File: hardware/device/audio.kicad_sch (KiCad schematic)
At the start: 33 parts, among them J4 HP_OUT, J5 AUDIO_EXP, J8 LINE_OUT, J9 LINE_IN, U24 MIC, U28 TS5A23159RSE, U29 NAU88C22YG, U30 TS5A23159RSE

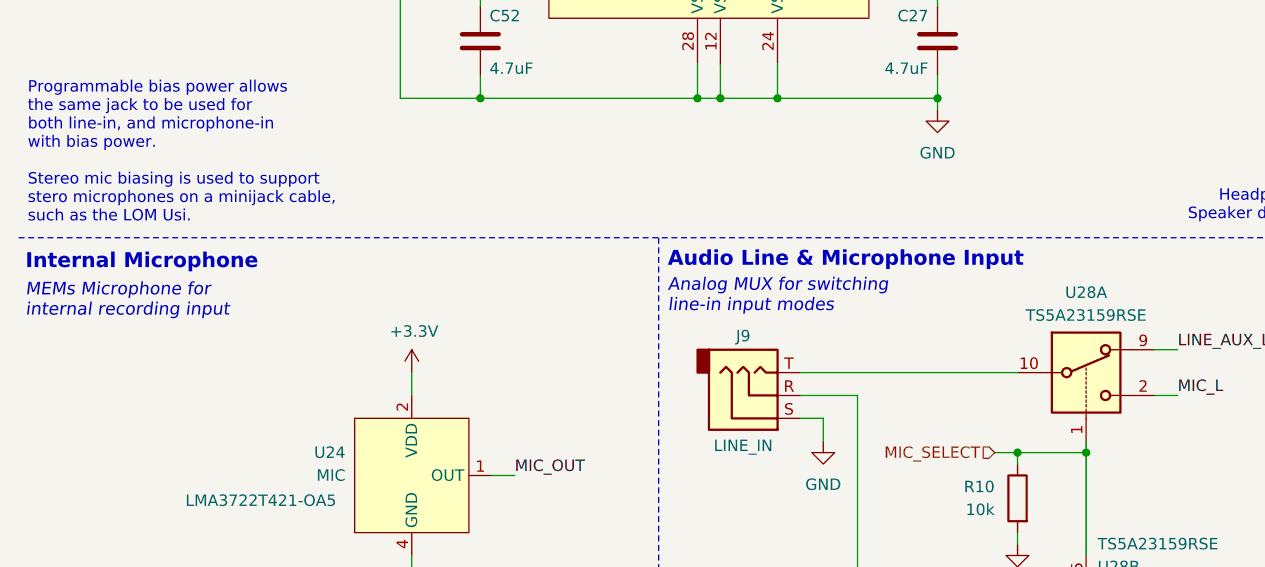
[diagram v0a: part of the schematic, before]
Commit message: feat: start routing keyswitch pads
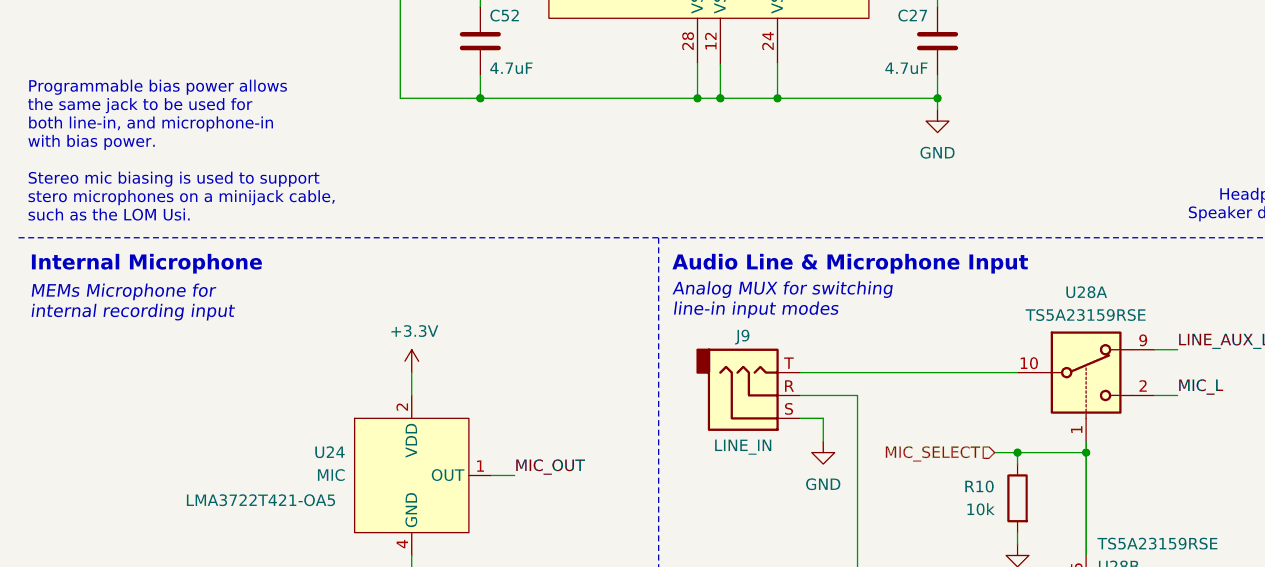
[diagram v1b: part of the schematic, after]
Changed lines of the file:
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@@
 	(text "MEMs Microphone for\ninternal recording input"
 		(exclude_from_sim no)
-		(at 12.954 151.384 0)
+		(at 13.462 151.638 0)
 		(effects
 			(font
@@
 	(text "Analog MUX for switching\nline-in input modes"
 		(exclude_from_sim no)
-		(at 84.328 150.876 0)
+		(at 84.836 151.384 0)
 		(effects
 			(font
@@
 	(text "Audio Line & Microphone Input"
 		(exclude_from_sim no)
-		(at 84.328 147.828 0)
+		(at 84.836 148.336 0)
 		(effects
 			(font
@@
 	(text "Internal Microphone"
 		(exclude_from_sim no)
-		(at 12.954 148.082 0)
-		(effects
-			(font
+		(at 13.462 148.336 0)
+		(effects
+			(font

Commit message: feat: audio system routing
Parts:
- removed C8: 0.1uF, Capacitor_SMD:C_0201_0603Metric, symbol Device:C_Small
- removed R11: 10k, Resistor_SMD:R_0201_0603Metric, symbol Device:R
- removed U30: TS5A23159RSE, Package_DFN_QFN:Texas_R-PUQFN-N10, symbol Analog_Switch:TS5A23159RSE
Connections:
- net LINE_AUX_L is gone; now on net AUX_L: U28.9
- net LINE_AUX_R is gone; now on net AUX_R: U28.7
- net CODEC.ADCDAT: no longer J5.5
- net CODEC.BCLK: no longer J5.9
- net CODEC.DACDAT: no longer J5.3
- net CODEC.LRCLK: no longer J5.7
- net CODEC.MCLK: no longer J5.11
- net EXP_CODEC.ADCDAT: now also J5.5; no longer J5.12
- net EXP_CODEC.BCLK: now also J5.9; no longer J5.16
- net EXP_CODEC.DACDAT: now also J5.3; no longer J5.10
- net EXP_CODEC.LRCLK: now also J5.7; no longer J5.14
- net EXP_CODEC.MCLK: now also J5.11; no longer J5.18
- net CODEC_IRQ: now reaches U29.6 (RLIN/GPIO3)
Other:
- note removed: "Aux-In Selection"

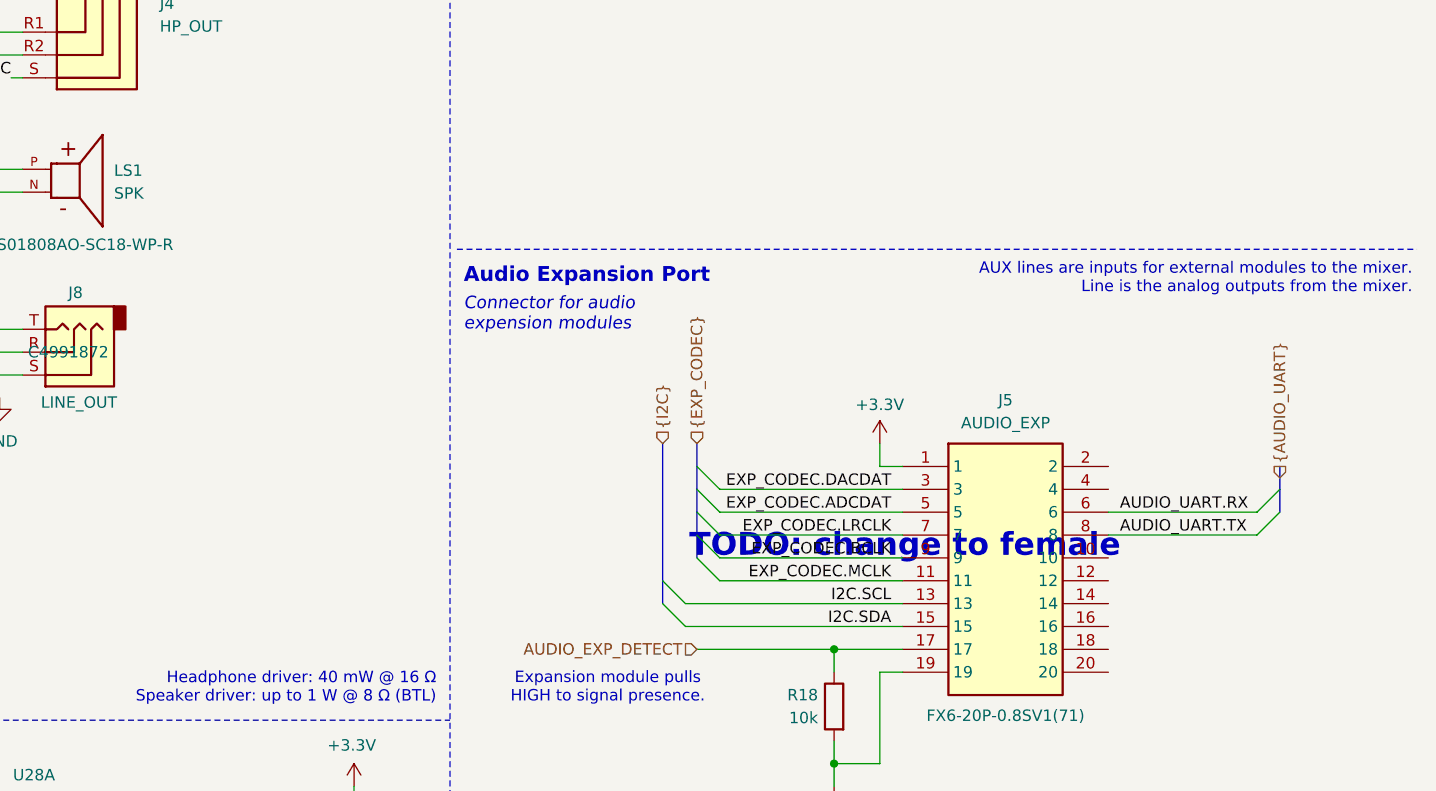
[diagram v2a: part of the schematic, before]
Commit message: feat: various routing, footprint and schematic cleanup
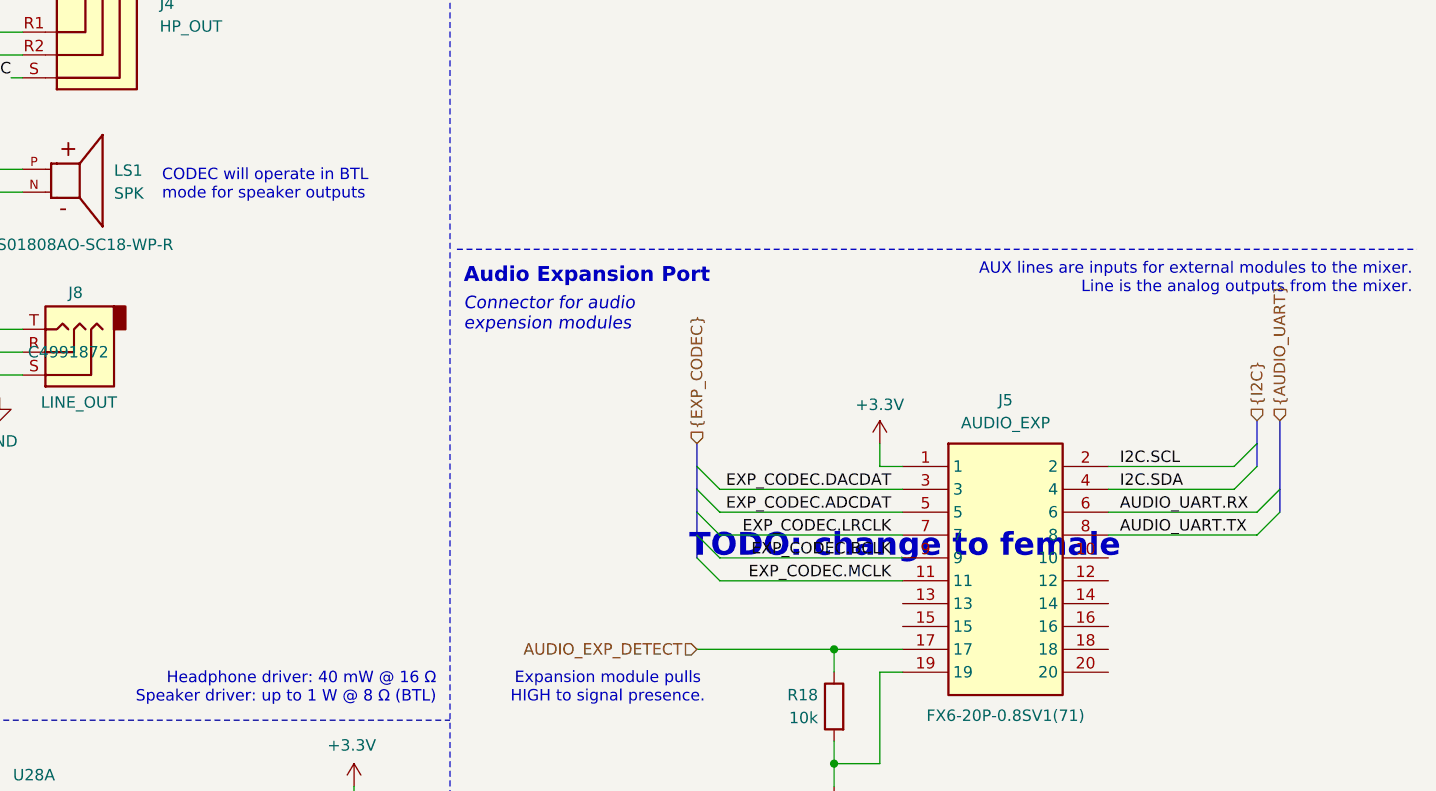
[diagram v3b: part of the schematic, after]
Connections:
- net I2C.SCL: now also J5.2; no longer J5.13
- net I2C.SDA: now also J5.4; no longer J5.15
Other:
- note added: "CODEC will operate in BTL mode for speaker outputs"
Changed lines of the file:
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@@
+		)
+	)
+	(text "CODEC will operate in BTL\nmode for speaker outputs"
+		(exclude_from_sim no)
+		(at 145.034 86.868 0)
+		(effects
+			(font
+				(size 1.27 1.27)
+				(color 132 132 132 1)
+			)
+			(justify left)
 		)
 	)
@@
 	)
 	(bus_entry
-		(at 203.2 133.35)
-		(size -2.54 -2.54)
+		(at 264.16 118.11)
+		(size 2.54 -2.54)
 		(stroke
 			(width 0)
@@
 	)
 	(bus_entry
-		(at 203.2 135.89)
-		(size -2.54 -2.54)
+		(at 264.16 120.65)
+		(size 2.54 -2.54)
 		(stroke
 			(width 0)
@@
 	(wire
 		(pts
-			(xy 203.2 135.89) (xy 227.33 135.89)
-		)
-		(stroke
-			(width 0)
-			(type default)
-		)
-	)
-	(wire
-		(pts
 			(xy 82.55 26.67) (xy 73.66 26.67)
 		)
@@
 		)
 	)
+	(wire
+		(pts
+			(xy 264.16 120.65) (xy 250.19 120.65)
+		)
+		(stroke
+			(width 0)
+			(type default)
+		)
+	)
 	(bus
 		(pts
-			(xy 200.66 115.57) (xy 200.66 130.81)
+			(xy 266.7 113.03) (xy 266.7 115.57)
 		)
 		(stroke
@@
 	(bus
 		(pts
-			(xy 200.66 130.81) (xy 200.66 133.35)
+			(xy 266.7 115.57) (xy 266.7 118.11)
 		)
 		(stroke
@@
 	(bus
 		(pts
-			(xy 269.24 118.11) (xy 269.24 120.65)
+			(xy 269.24 113.03) (xy 269.24 120.65)
 		)
 		(stroke
@@
 	(wire
 		(pts
-			(xy 203.2 133.35) (xy 227.33 133.35)
+			(xy 264.16 118.11) (xy 250.19 118.11)
 		)
 		(stroke
@@
 	)
 	(label "I2C.SCL"
-		(at 226.06 133.35 180)
-		(effects
-			(font
-				(size 1.27 1.27)
-			)
-			(justify right bottom)
+		(at 251.46 118.11 0)
+		(effects
+			(font
+				(size 1.27 1.27)
+			)
+			(justify left bottom)
 		)
 	)
@@
 	)
 	(label "I2C.SDA"
-		(at 226.06 135.89 180)
-		(effects
-			(font
-				(size 1.27 1.27)
-			)
-			(justify right bottom)
+		(at 251.46 120.65 0)
+		(effects
+			(font
+				(size 1.27 1.27)
+			)
+			(justify left bottom)
 		)
 	)
@@
 	(hierarchical_label "{AUDIO_UART}"
 		(shape input)
-		(at 269.24 119.38 90)
+		(at 269.24 113.03 90)
 		(effects
 			(font
@@
 	(hierarchical_label "{I2C}"
 		(shape input)
-		(at 200.66 115.57 90)
-		(effects
-			(font
+		(at 266.7 113.03 90)
+		(effects
+			(font

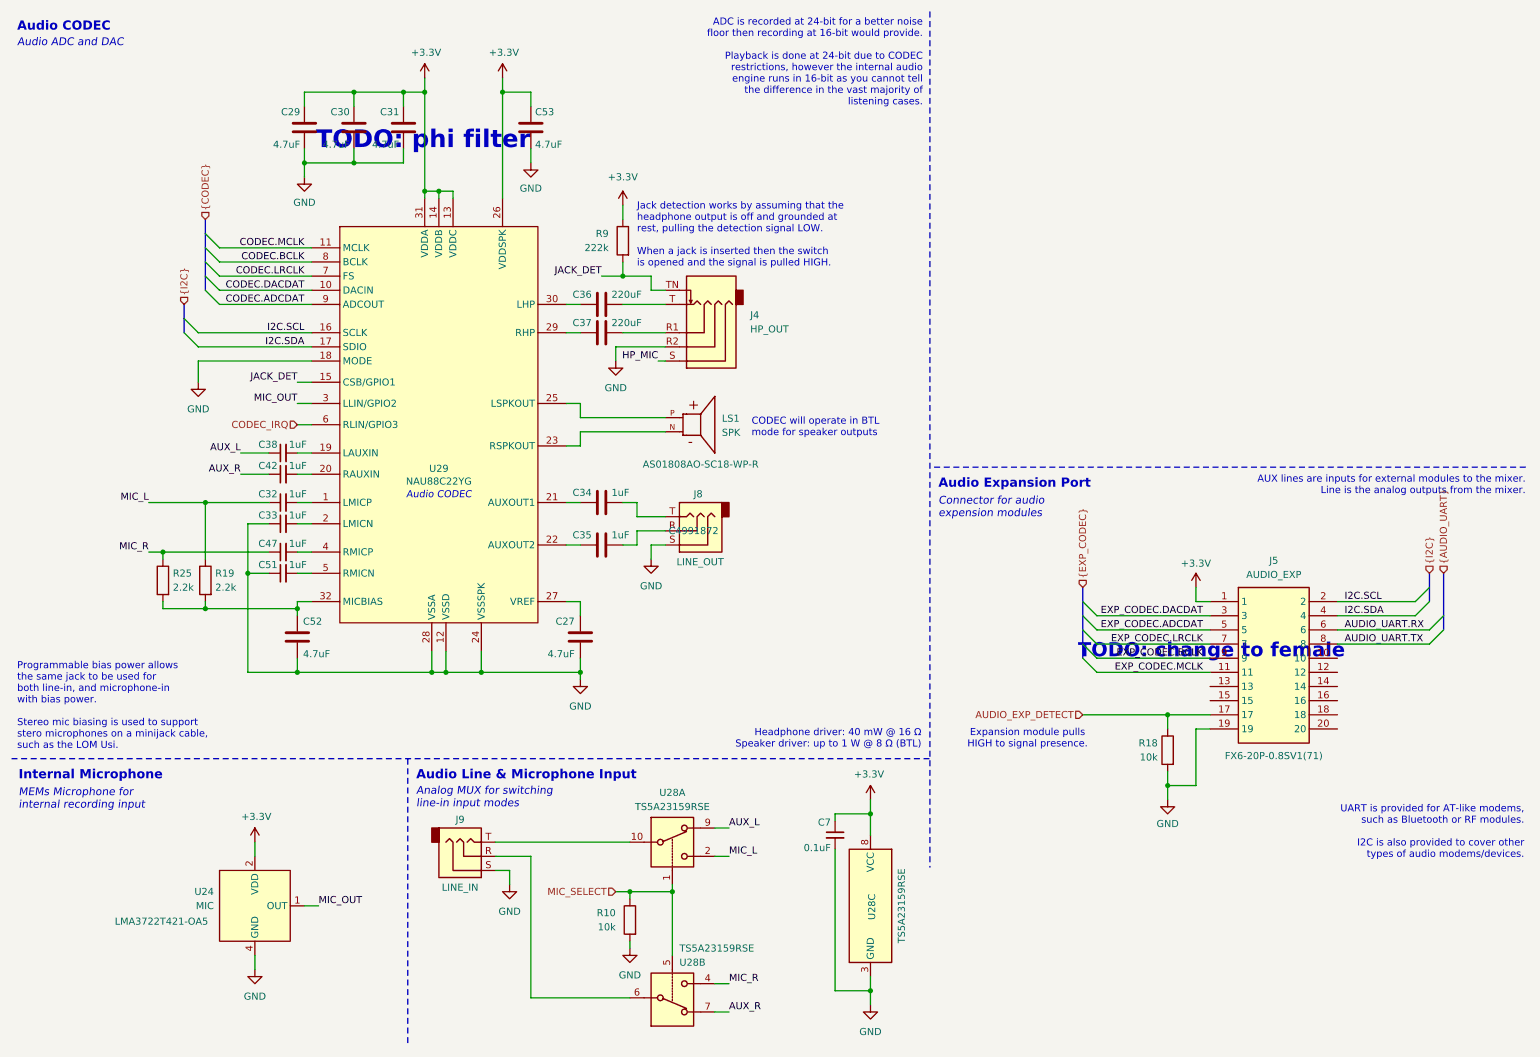
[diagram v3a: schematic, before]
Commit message: feat: start replacing expansion  port with bluetooth module
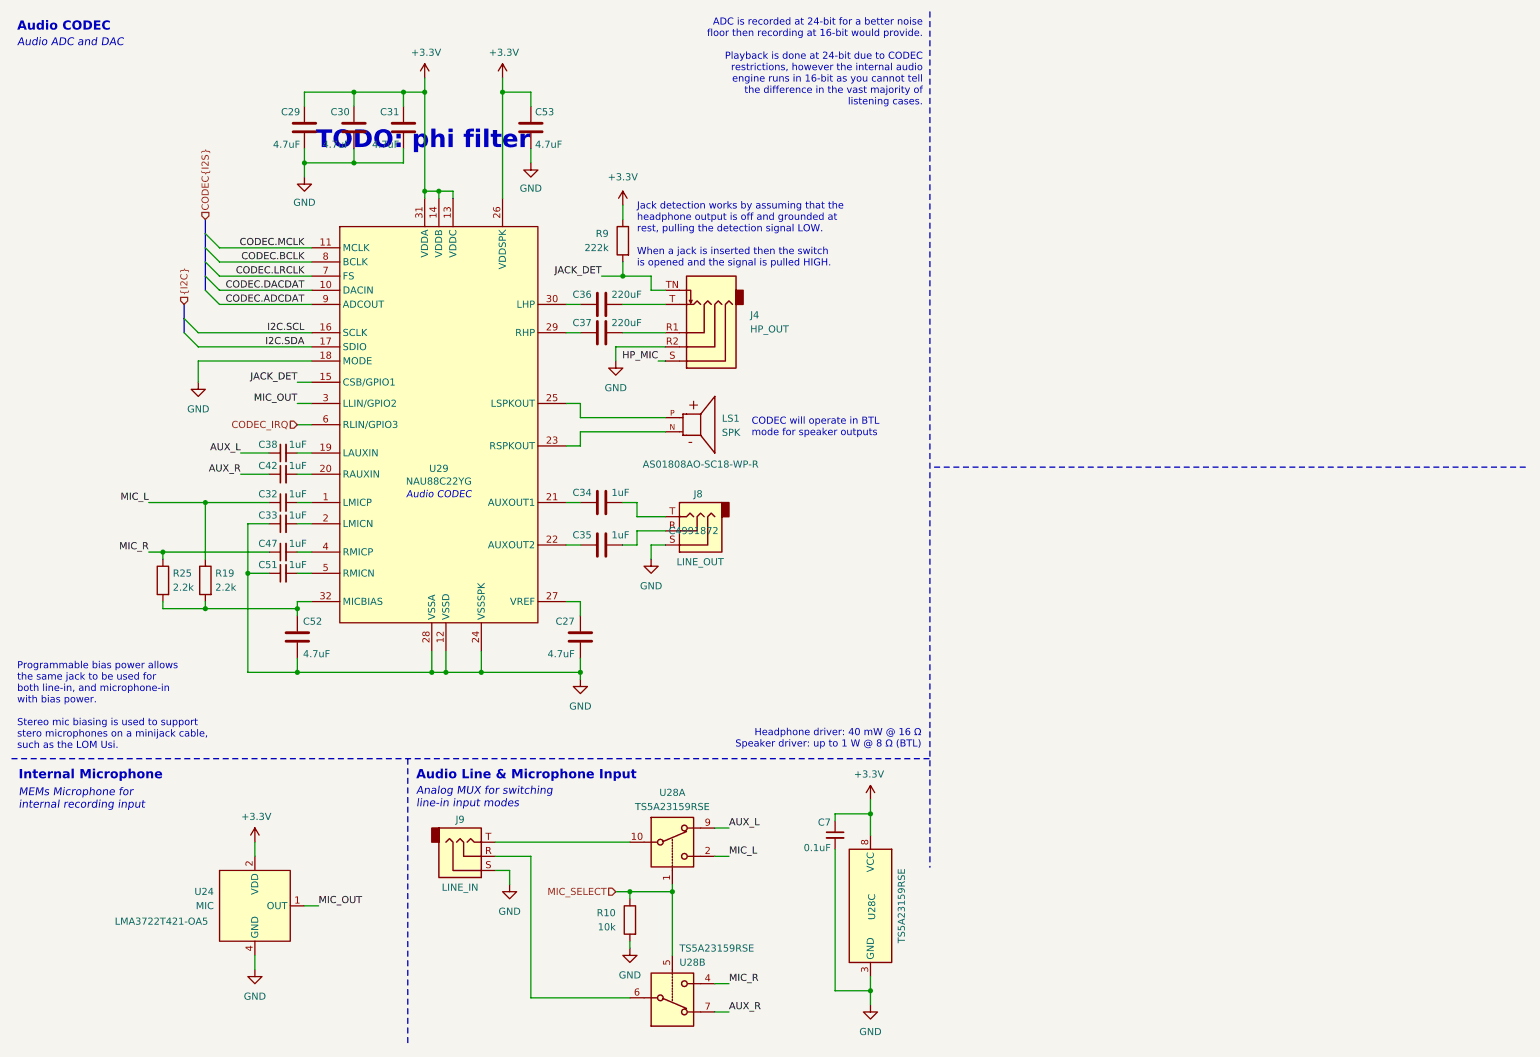
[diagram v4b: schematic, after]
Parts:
- removed J5: AUDIO_EXP, pocket_synth:FX6-20P-0.8SV1(71), symbol pocket_synth:FX6-20P-0.8SV1(71)
- removed R18: 10k, Resistor_SMD:R_0201_0603Metric, symbol Device:R
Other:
- note removed: "AUX lines are inputs for external modules to the mixer. Line is the analog outputs from the mixer."
- note removed: "Audio Expansion Port"
- note removed: "Connector for audio expension modules"
- note removed: "Expansion module pulls HIGH to signal presence."
- note removed: "TODO: change to female"
- note removed: "UART is provided for AT-like modems, such as Bluetooth or RF modules. I2C is also provided to cover other types of audio modems/devices."

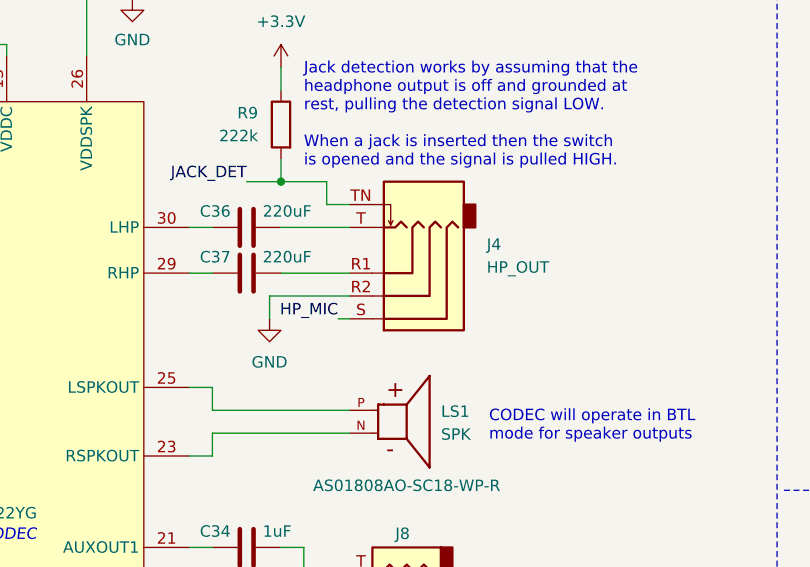
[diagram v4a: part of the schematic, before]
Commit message: feat: start adding headphone jack connector
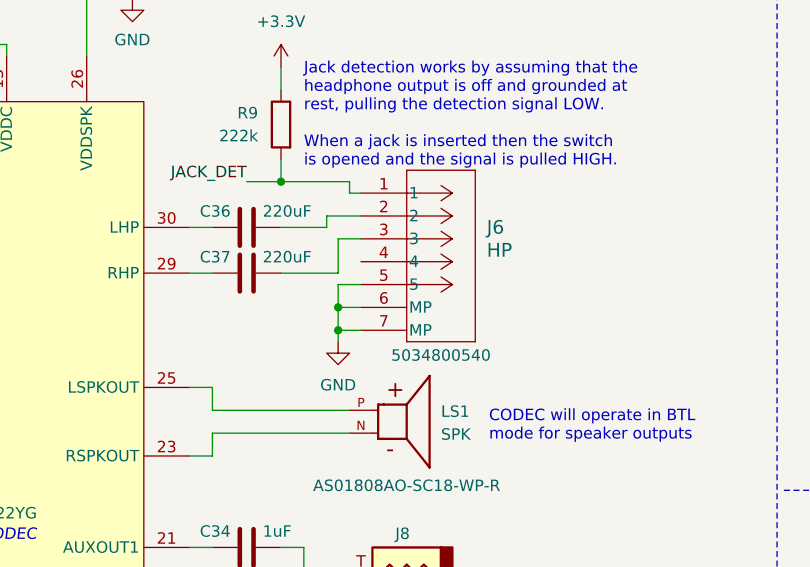
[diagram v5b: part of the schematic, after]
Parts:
- removed J4: HP_OUT, symbol Connector_Audio:AudioJack4_SwitchT1
- added J6: HP, pocket_synth:CONN_503480-0540_MOL, symbol pocket_synth:5034800540
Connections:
- net GND: now also J6.5, J6.6 (MP), J6.7 (MP)
- net JACK_DET: now also J6.1
- net at C37.2: now also J6.3
- net at C36.2: now also J6.2
